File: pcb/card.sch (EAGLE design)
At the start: 24 parts, among them IC1 74HC14D, IC2 24LC256SN, Q1 BC817

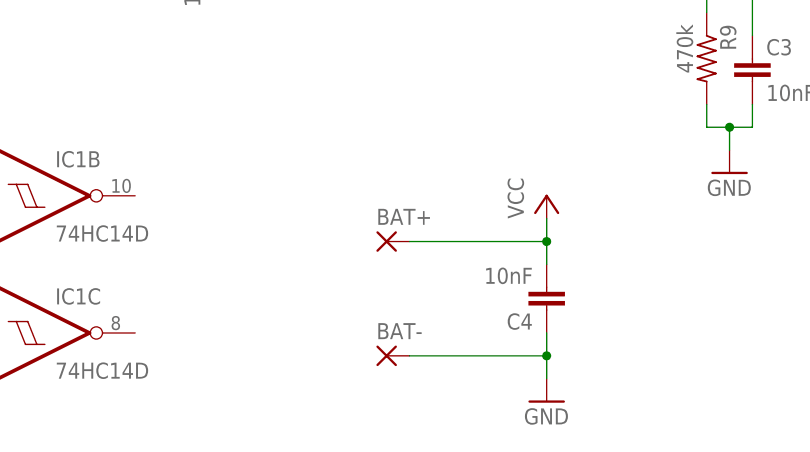
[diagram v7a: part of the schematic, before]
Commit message: Added the battery holder to the schematic.
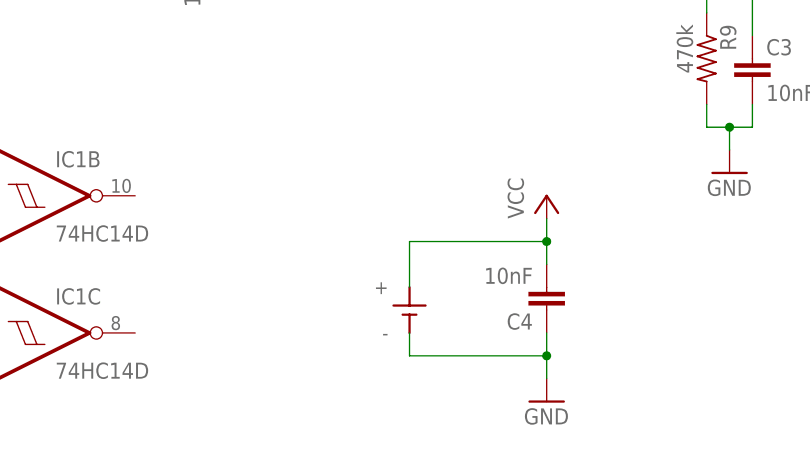
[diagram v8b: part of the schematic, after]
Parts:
- removed BAT+, BAT-: (no value), wirepad:SMD2
- added BAT: KB3003, bat:KB3003
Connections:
- net GND: now also BAT.-; no longer BAT-.P
- net VCC: now also BAT.+; no longer BAT+.P
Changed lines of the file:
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@@
 <grid distance="0.1" unitdist="inch" unit="inch" style="lines" multiple="1" display="no" altdistance="0.01" altunitdist="inch" altunit="inch"/>
 <layers>
-<layer number="1" name="Top" color="4" fill="1" visible="yes" active="no"/>
-<layer number="16" name="Bottom" color="1" fill="1" visible="yes" active="no"/>
-<layer number="17" name="Pads" color="2" fill="1" visible="yes" active="no"/>
-<layer number="18" name="Vias" color="2" fill="1" visible="yes" active="no"/>
-<layer number="19" name="Unrouted" color="6" fill="1" visible="yes" active="no"/>
-<layer number="20" name="Dimension" color="15" fill="1" visible="yes" active="no"/>
-<layer number="21" name="tPlace" color="7" fill="1" visible="yes" active="no"/>
-<layer number="22" name="bPlace" color="7" fill="1" visible="yes" active="no"/>
-<layer number="23" name="tOrigins" color="15" fill="1" visible="yes" active="no"/>
-<layer number="24" name="bOrigins" color="15" fill="1" visible="yes" active="no"/>
-<layer number="25" name="tNames" color="7" fill="1" visible="yes" active="no"/>
-<layer number="26" name="bNames" color="7" fill="1" visible="yes" active="no"/>
-<layer number="27" name="tValues" color="7" fill="1" visible="yes" active="no"/>
-<layer number="28" name="bValues" color="7" fill="1" visible="yes" active="no"/>
+<layer number="1" name="Top" color="4" fill="1" visible="no" active="no"/>
+<layer number="16" name="Bottom" color="1" fill="1" visible="no" active="no"/>
+<layer number="17" name="Pads" color="2" fill="1" visible="no" active="no"/>
+<layer number="18" name="Vias" color="2" fill="1" visible="no" active="no"/>
+<layer number="19" name="Unrouted" color="6" fill="1" visible="no" active="no"/>
+<layer number="20" name="Dimension" color="15" fill="1" visible="no" active="no"/>
+<layer number="21" name="tPlace" color="7" fill="1" visible="no" active="no"/>
+<layer number="22" name="bPlace" color="7" fill="1" visible="no" active="no"/>
+<layer number="23" name="tOrigins" color="15" fill="1" visible="no" active="no"/>
+<layer number="24" name="bOrigins" color="15" fill="1" visible="no" active="no"/>
+<layer number="25" name="tNames" color="7" fill="1" visible="no" active="no"/>
+<layer number="26" name="bNames" color="7" fill="1" visible="no" active="no"/>
+<layer number="27" name="tValues" color="7" fill="1" visible="no" active="no"/>
+<layer number="28" name="bValues" color="7" fill="1" visible="no" active="no"/>
 <layer number="29" name="tStop" color="7" fill="3" visible="no" active="no"/>
 <layer number="30" name="bStop" color="7" fill="6" visible="no" active="no"/>
@@
 <layer number="35" name="tGlue" color="7" fill="4" visible="no" active="no"/>
 <layer number="36" name="bGlue" color="7" fill="5" visible="no" active="no"/>
-<layer number="37" name="tTest" color="7" fill="1" visible="yes" active="no"/>
-<layer number="38" name="bTest" color="7" fill="1" visible="yes" active="no"/>
+<layer number="37" name="tTest" color="7" fill="1" visible="no" active="no"/>
+<layer number="38" name="bTest" color="7" fill="1" visible="no" active="no"/>
 <layer number="39" name="tKeepout" color="4" fill="11" visible="no" active="no"/>
 <layer number="40" name="bKeepout" color="1" fill="11" visible="no" active="no"/>
@@
 <layer number="44" name="Drills" color="7" fill="1" visible="no" active="no"/>
 <layer number="45" name="Holes" color="7" fill="1" visible="no" active="no"/>
-<layer number="46" name="Milling" color="3" fill="1" visible="yes" active="no"/>
-<layer number="47" name="Measures" color="7" fill="1" visible="yes" active="no"/>
-<layer number="48" name="Document" color="7" fill="1" visible="yes" active="no"/>
-<layer number="49" name="Reference" color="7" fill="1" visible="yes" active="no"/>
-<layer number="51" name="tDocu" color="7" fill="1" visible="yes" active="no"/>
-<layer number="52" name="bDocu" color="7" fill="1" visible="yes" active="no"/>
+<layer number="46" name="Milling" color="3" fill="1" visible="no" active="no"/>
+<layer number="47" name="Measures" color="7" fill="1" visible="no" active="no"/>
+<layer number="48" name="Document" color="7" fill="1" visible="no" active="no"/>
+<layer number="49" name="Reference" color="7" fill="1" visible="no" active="no"/>
+<layer number="51" name="tDocu" color="7" fill="1" visible="no" active="no"/>
+<layer number="52" name="bDocu" color="7" fill="1" visible="no" active="no"/>
 <layer number="90" name="Modules" color="5" fill="1" visible="yes" active="yes"/>
 <layer number="91" name="Nets" color="2" fill="1" visible="yes" active="yes"/>
@@
 <part name="SDA" library="wirepad" deviceset="SMD2" device=""/>
 <part name="SCL" library="wirepad" deviceset="SMD2" device=""/>
-<part name="BAT+" library="wirepad" deviceset="SMD2" device=""/>
-<part name="BAT-" library="wirepad" deviceset="SMD2" device=""/>
 <part name="IC2" library="microchip" deviceset="24*" device="SN" technology="LC256"/>
 <part name="GND" library="wirepad" deviceset="SMD2" device=""/>
@@
 <part name="R5" library="resistor" deviceset="R-US_" device="M1206" value="10M"/>
 <part name="ANT" library="testpad" deviceset="TP" device="B1,27"/>
+<part name="BAT" library="bat" deviceset="KB3003" device=""/>
 </parts>
 <sheets>
@@
 <instance part="SDA" gate="1" x="134.62" y="15.24" rot="R180"/>
 <instance part="SCL" gate="1" x="93.98" y="22.86"/>
-<instance part="BAT+" gate="1" x="43.18" y="17.78"/>
-<instance part="BAT-" gate="1" x="43.18" y="5.08"/>
 <instance part="IC2" gate="G$1" x="114.3" y="15.24"/>
 <instance part="GND" gate="1" x="93.98" y="15.24"/>
@@
 <instance part="R5" gate="G$1" x="-22.86" y="22.86" rot="R180"/>
 <instance part="ANT" gate="G$1" x="-17.78" y="78.74"/>
+<instance part="BAT" gate="G$1" x="45.72" y="10.16"/>
 </instances>
 <busses>
@@
 <wire x1="45.72" y1="5.08" x2="60.96" y2="5.08" width="0.1524" layer="91"/>
 <junction x="60.96" y="5.08"/>
-<pinref part="BAT-" gate="1" pin="P"/>
+<pinref part="BAT" gate="G$1" pin="-"/>
+<wire x1="45.72" y1="5.08" x2="45.72" y2="7.62" width="0.1524" layer="91"/>
 </segment>
 <segment>
@@
 <wire x1="45.72" y1="17.78" x2="60.96" y2="17.78" width="0.1524" layer="91"/>
 <junction x="60.96" y="17.78"/>
-<pinref part="BAT+" gate="1" pin="P"/>
-</segment>
-<segment>
+<pinref part="BAT" gate="G$1" pin="+"/>
+<wire x1="45.72" y1="17.78" x2="45.72" y2="12.7" width="0.1524" layer="91"/>
+</segment>
+<segment>
